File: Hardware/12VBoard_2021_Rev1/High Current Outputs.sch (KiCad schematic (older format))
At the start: 6 parts

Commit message: fixed things
project folders, IC symbol size, library
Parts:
- removed U?: BD9611MUV, symbol Converter_DCDC:BD9611MUV
- added U?: BD9611MUV, symbol 12VBoard_2021_Rev1:BD9611MUV
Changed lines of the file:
@@
 EESchema Schematic File Version 4
+LIBS:12VBoard_2021_Rev1-cache
 EELAYER 30 0
 EELAYER END
@@
 Comment4 ""
 $EndDescr
-$Comp
-L Converter_DCDC:BD9611MUV U?
-U 1 1 5F7A443F
-P 2800 2300
-F 0 "U?" H 2800 2400 50  0000 C CNN
-F 1 "BD9611MUV" H 2800 2300 50  0000 C CNN
-F 2 "" H 2800 2450 50  0001 C CNN
-F 3 "" H 2800 2450 50  0001 C CNN
-	1    2800 2300
-	1    0    0    -1
-$EndComp
 $Comp
 L power:+12V #PWR?
@@
 	0    -1   -1   0
 $EndComp
+$Comp
+L 12VBoard_2021_Rev1:BD9611MUV U?
+U 1 1 5F7A09D5
+P 2550 1400
+F 0 "U?" H 2550 2200 50  0000 C CNN
+F 1 "BD9611MUV" H 2550 2000 50  0000 C CNN
+F 2 "" H 2550 1400 50  0001 C CNN
+F 3 "" H 2550 1400 50  0001 C CNN
+	1    2550 1400
+	1    0    0    -1
+$EndComp
 $EndSCHEMATC

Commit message: Finished layingout componets needed for buck converter
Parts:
- removed C? (x3): 0.1uF, symbol pspice:CAP
- added C? (x6): 10uF, symbol pspice:CAP
- added C?: 0.47uF, symbol pspice:CAP
- added C? (x2): 1uF, symbol pspice:CAP
- added C? (x2): 0.01uF, symbol pspice:CAP
- added C?: 2200pF, symbol pspice:CAP
- added C?: 180pF, symbol pspice:CAP
- added C?: 220uF, symbol Device:CP1
- added L?: L, symbol Device:L
- added Q? (x2): NTR2101P, Package_TO_SOT_SMD:SOT-23, symbol Transistor_FET:NTR2101P
- added R? (x2): R, symbol Device:R
- added R?: 15K, symbol Device:R
- added R?: 1k, symbol Device:R
- added R?: 140k, symbol Device:R
- added R?: 10k, symbol Device:R
- added R?: 75k, symbol Device:R
- U?: symbol 12VBoard_2021_Rev1:BD9611MUV -> 12VBoard_2021_Rev1-rescue:BD9611MUV-12VBoard_2021_Rev1
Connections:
- net labels added: CSout, CTL1, FB, GND, HG, INV, LG, NchMID, Power, Vo
- wire segments 0 -> 70
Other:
- moved on the sheet: C?

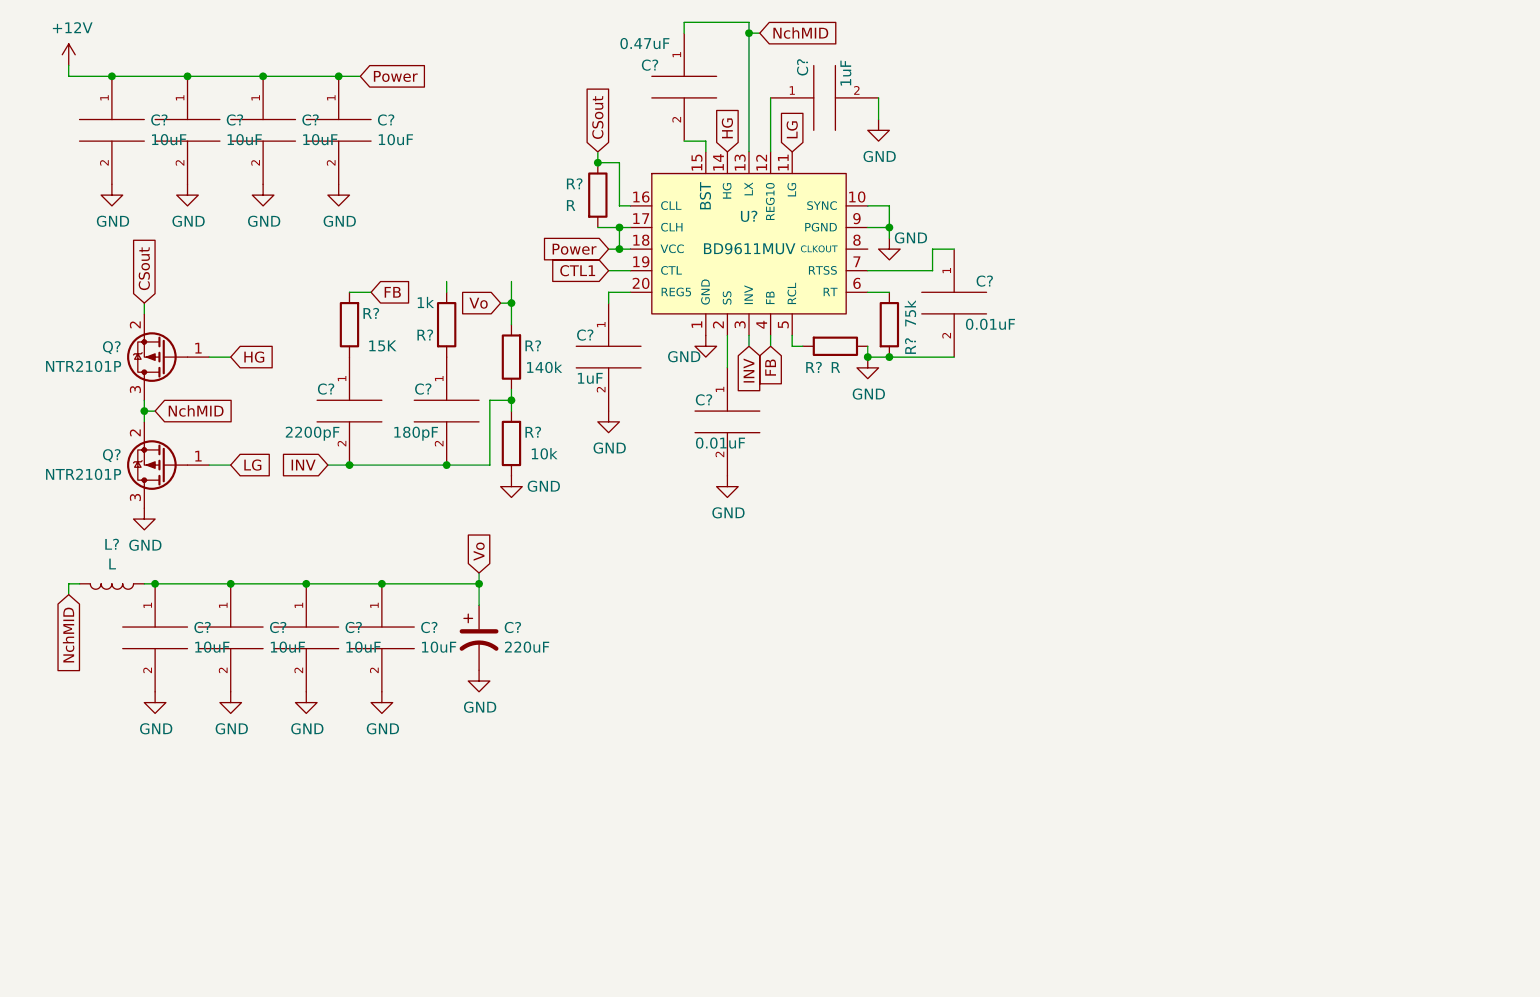
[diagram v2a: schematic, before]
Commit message: Created Buck Circuts
added boxes that Dan hates
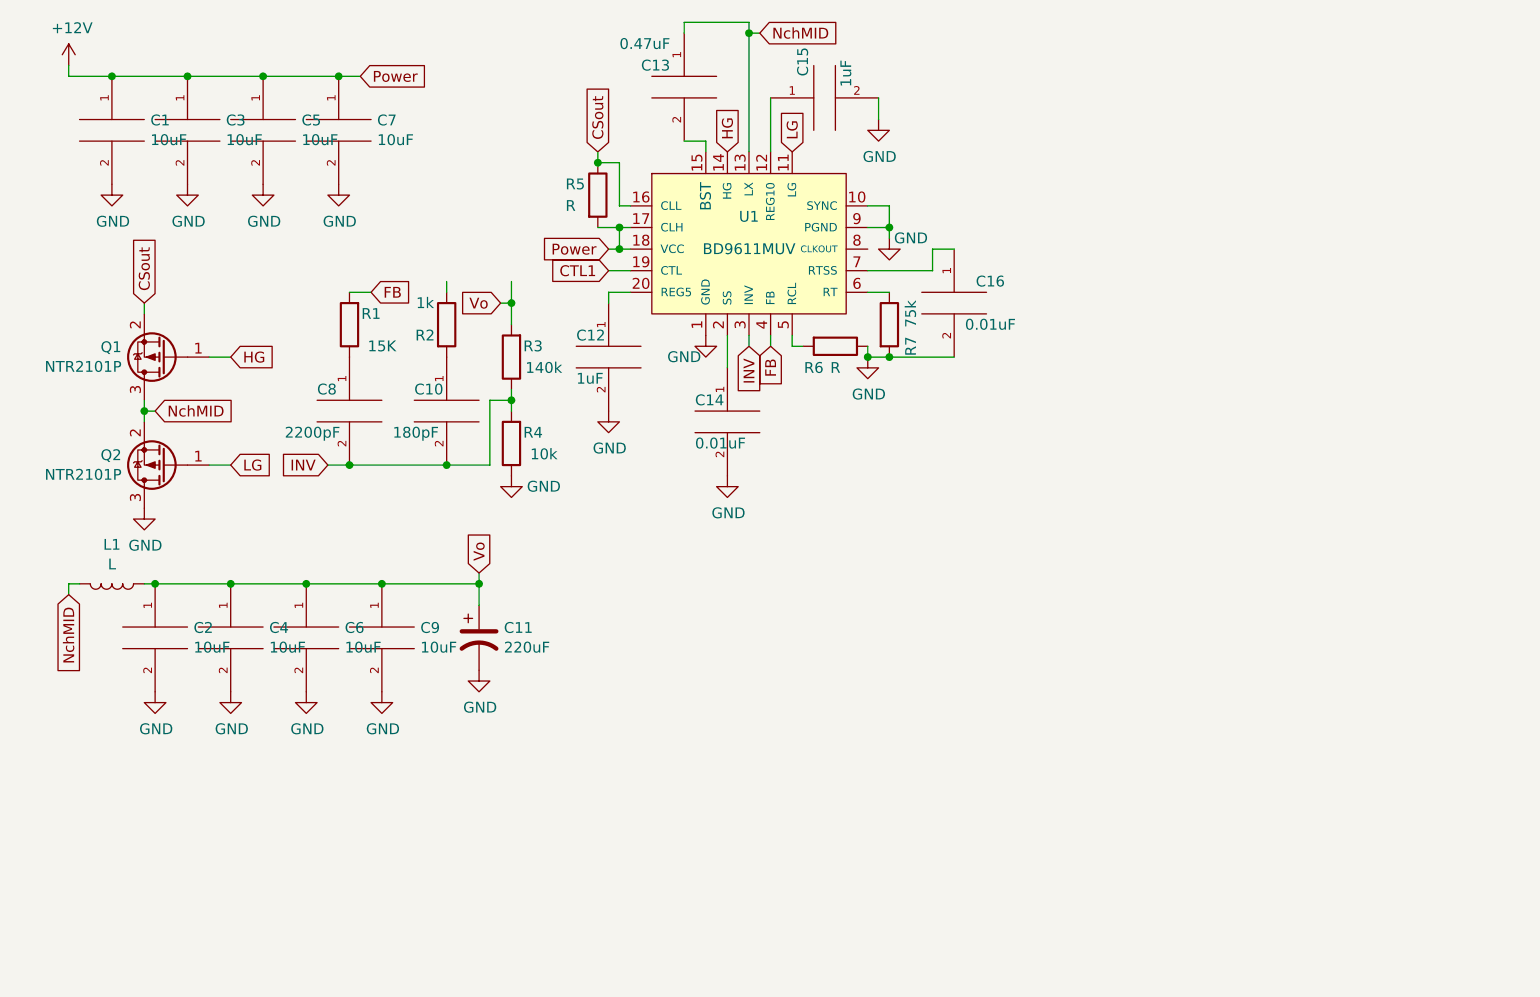
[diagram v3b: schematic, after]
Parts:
- gave numbers to parts that had none: 27

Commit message: High current
Hiearchial setup of high current. started working on high current setup with anderson.
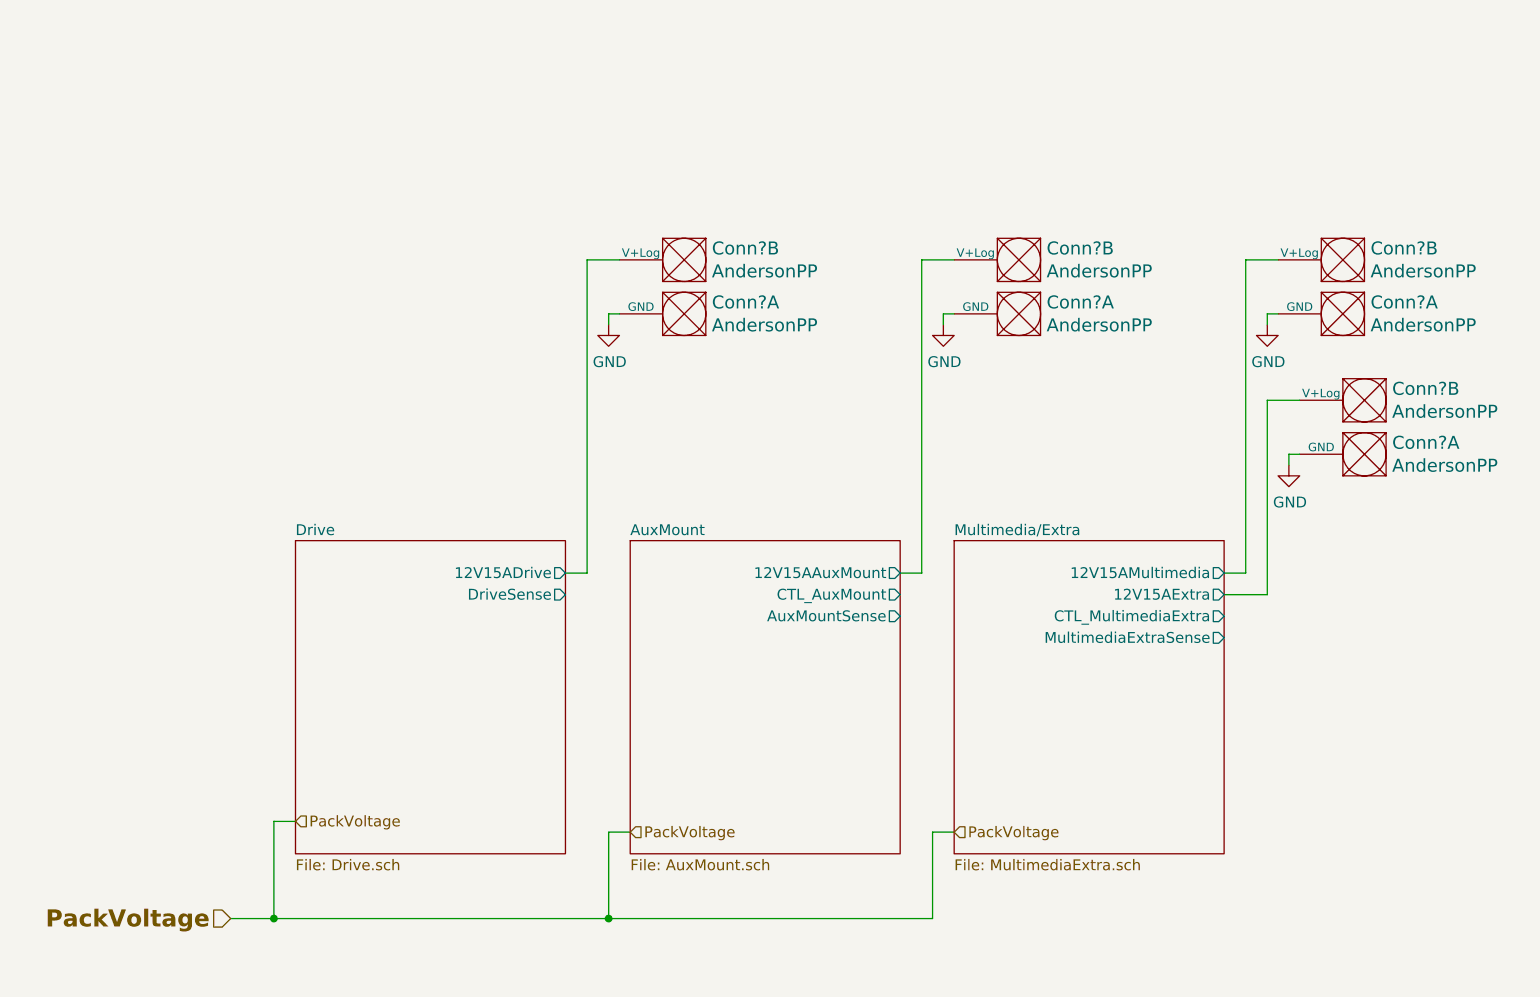
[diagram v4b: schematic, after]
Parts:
- removed C1, C2, C3, C4, C5, C6, C7, C9: 10uF, symbol pspice:CAP
- removed C10: 180pF, symbol pspice:CAP
- removed C11: 220uF, symbol Device:CP1
- removed C12, C15: 1uF, symbol pspice:CAP
- removed C13: 0.47uF, symbol pspice:CAP
- removed C14, C16: 0.01uF, symbol pspice:CAP
- removed C8: 2200pF, symbol pspice:CAP
- removed L1: L, symbol Device:L
- removed Q1, Q2: NTR2101P, Package_TO_SOT_SMD:SOT-23, symbol Transistor_FET:NTR2101P
- removed R1: 15K, symbol Device:R
- removed R2: 1k, symbol Device:R
- removed R3: 140k, symbol Device:R
- removed R4: 10k, symbol Device:R
- removed R5, R6: R, symbol Device:R
- removed R7: 75k, symbol Device:R
- removed U1: BD9611MUV, symbol 12VBoard_2021_Rev1-rescue:BD9611MUV-12VBoard_2021_Rev1
- added Conn? (x8): AndersonPP, symbol MRDT_Connectors:AndersonPP
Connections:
- net labels added: PackVoltage
- net labels removed: +12V, CSout, CTL1, FB, HG, INV, LG, NchMID, Power, Vo
- wire segments 70 -> 29

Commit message: High current
Fisnished adding labes/tags
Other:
- note added: "Delete Drive"
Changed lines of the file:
@@
 F2 "12V15ADrive" O R 2950 3100 50
 F3 "DriveSense" O R 2950 3200 50
-$EndSheet
-$Sheet
-S 3250 2950 1250 1450
-U 5F8222BE
-F0 "AuxMount" 50
-F1 "AuxMount.sch" 50
-F2 "12V15AAuxMount" O R 4500 3100 50
-F3 "CTL_AuxMount" O R 4500 3200 50
-F4 "AuxMountSense" O R 4500 3300 50
+F4 "5V" O L 1700 4150 49
 $EndSheet
 $Sheet
@@
 F4 "12V15AExtra" O R 6000 3200 50
 F5 "MultimediaExtraSense" O R 6000 3400 50
+F6 "5V" O L 4750 4200 49
 $EndSheet
 $Comp
@@
 Wire Wire Line
 	6200 3200 6200 2300
+Text HLabel 1400 4900 0    79   Input ~ 16
+5V
+$Sheet
+S 3250 2950 1250 1450
+U 5F8222BE
+F0 "AuxMount" 50
+F1 "AuxMount.sch" 50
+F2 "12V15AAuxMount" O R 4500 3100 50
+F3 "CTL_AuxMount" O R 4500 3200 50
+F4 "AuxMountSense" O R 4500 3300 50
+F5 "5V" O L 3250 4200 49
+$EndSheet
+Wire Wire Line
+	1400 4900 1550 4900
+Wire Wire Line
+	4600 4900 4600 4200
+Wire Wire Line
+	4600 4200 4750 4200
+Wire Wire Line
+	3250 4200 3100 4200
+Wire Wire Line
+	3100 4200 3100 4900
+Connection ~ 3100 4900
+Wire Wire Line
+	3100 4900 4600 4900
+Wire Wire Line
+	1700 4150 1550 4150
+Wire Wire Line
+	1550 4150 1550 4900
+Connection ~ 1550 4900
+Wire Wire Line
+	1550 4900 3100 4900
+Text Notes 1950 2700 0    79   ~ 16
+Delete Drive
+Text HLabel 4650 3350 3    49   Output ~ 0
+AuxCTL
+Text HLabel 4550 3350 3    49   Output ~ 0
+AuxMountSense
+Wire Wire Line
+	4550 3350 4550 3300
+Wire Wire Line
+	4550 3300 4500 3300
+Wire Wire Line
+	4500 3200 4650 3200
+Wire Wire Line
+	4650 3200 4650 3350
+Text HLabel 6050 3450 3    49   Input ~ 0
+MultimediaSense
+Text HLabel 6150 3450 3    49   Output ~ 0
+MultimediaCTL
+Wire Wire Line
+	6050 3450 6050 3400
+Wire Wire Line
+	6050 3400 6000 3400
+Wire Wire Line
+	6000 3300 6150 3300
+Wire Wire Line
+	6150 3300 6150 3450
+Text HLabel 3000 3250 3    49   Input ~ 0
+DriveSense
+Wire Wire Line
+	3000 3250 3000 3200
+Wire Wire Line
+	3000 3200 2950 3200
 $EndSCHEMATC

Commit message: reviewed
review
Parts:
- removed Conn? (x2): AndersonPP, symbol MRDT_Connectors:AndersonPP
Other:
- note removed: "Delete Drive"
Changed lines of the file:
@@
 $Descr A4 11693 8268
 encoding utf-8
-Sheet 5 8
+Sheet 5 7
 Title ""
 Date ""
@@
 Text HLabel 1400 4700 0    79   Input ~ 16
 PackVoltage
-Text HLabel 1700 4250 2    50   Input ~ 0
-PackVoltage
 Text HLabel 3250 4300 2    50   Input ~ 0
 PackVoltage
@@
 PackVoltage
 Wire Wire Line
-	1400 4700 1600 4700
-Wire Wire Line
-	1700 4250 1600 4250
-Wire Wire Line
-	1600 4250 1600 4700
-Connection ~ 1600 4700
-Wire Wire Line
 	4650 4700 4650 4300
 Wire Wire Line
 	4650 4300 4750 4300
-Wire Wire Line
-	1600 4700 3150 4700
 Wire Wire Line
 	3250 4300 3150 4300
@@
 Wire Wire Line
 	3150 4700 4650 4700
-$Sheet
-S 1700 2950 1250 1450
-U 5F821EB2
-F0 "Drive" 50
-F1 "Drive.sch" 50
-F2 "12V15ADrive" O R 2950 3100 50
-F3 "DriveSense" O R 2950 3200 50
-F4 "5V" O L 1700 4150 49
-$EndSheet
 $Sheet
 S 4750 2950 1250 1450
@@
 F6 "5V" O L 4750 4200 49
 $EndSheet
-$Comp
-L MRDT_Connectors:AndersonPP Conn?
-U 1 1 5F9BB8B5
-P 3600 1800
-AR Path="/5F74F36B/5F821EB2/5F9BB8B5" Ref="Conn?"  Part="1"
-AR Path="/5F74F36B/5F9BB8B5" Ref="Conn?"  Part="1"
-F 0 "Conn?" H 3572 1847 60  0000 R CNN
-F 1 "AndersonPP" H 3572 1953 60  0000 R CNN
-F 2 "" H 3450 1250 60  0001 C CNN
-F 3 "" H 3450 1250 60  0001 C CNN
-	1    3600 1800
-	-1   0    0    1
-$EndComp
-$Comp
-L MRDT_Connectors:AndersonPP Conn?
-U 2 1 5F9BB8BB
-P 3600 1550
-AR Path="/5F74F36B/5F821EB2/5F9BB8BB" Ref="Conn?"  Part="2"
-AR Path="/5F74F36B/5F9BB8BB" Ref="Conn?"  Part="2"
-F 0 "Conn?" H 3572 1597 60  0000 R CNN
-F 1 "AndersonPP" H 3572 1703 60  0000 R CNN
-F 2 "" H 3450 1000 60  0001 C CNN
-F 3 "" H 3450 1000 60  0001 C CNN
-	2    3600 1550
-	-1   0    0    1
-$EndComp
-$Comp
-L power:GND #PWR?
-U 1 1 5F9BB8C1
-P 3150 1950
-AR Path="/5F74F36B/5F821EB2/5F9BB8C1" Ref="#PWR?"  Part="1"
-AR Path="/5F74F36B/5F9BB8C1" Ref="#PWR?"  Part="1"
-F 0 "#PWR?" H 3150 1700 50  0001 C CNN
-F 1 "GND" H 3155 1777 50  0000 C CNN
-F 2 "" H 3150 1950 50  0001 C CNN
-F 3 "" H 3150 1950 50  0001 C CNN
-	1    3150 1950
-	1    0    0    -1
-$EndComp
-Wire Wire Line
-	3200 1900 3150 1900
-Wire Wire Line
-	3150 1900 3150 1950
-Wire Wire Line
-	2950 3100 3050 3100
-Wire Wire Line
-	3050 3100 3050 1650
-Wire Wire Line
-	3050 1650 3200 1650
 $Comp
 L MRDT_Connectors:AndersonPP Conn?
@@
 $EndSheet
 Wire Wire Line
-	1400 4900 1550 4900
-Wire Wire Line
 	4600 4900 4600 4200
 Wire Wire Line
@@
 Wire Wire Line
 	3100 4900 4600 4900
-Wire Wire Line
-	1700 4150 1550 4150
-Wire Wire Line
-	1550 4150 1550 4900
-Connection ~ 1550 4900
-Wire Wire Line
-	1550 4900 3100 4900
-Text Notes 1950 2700 0    79   ~ 16
-Delete Drive
 Text HLabel 4650 3350 3    49   Output ~ 0
 AuxCTL
@@
 Wire Wire Line
 	6150 3300 6150 3450
-Text HLabel 3000 3250 3    49   Input ~ 0
-DriveSense
-Wire Wire Line
-	3000 3250 3000 3200
-Wire Wire Line
-	3000 3200 2950 3200
+Wire Wire Line
+	1400 4700 3150 4700
+Wire Wire Line
+	1400 4900 3100 4900
 $EndSCHEMATC
